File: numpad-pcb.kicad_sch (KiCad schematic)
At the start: 20 parts, among them J1 AVR-ISP-6, SW1 SW_Push, U1 ATmega32U4-A, Y1 Crystal_GND24_Small

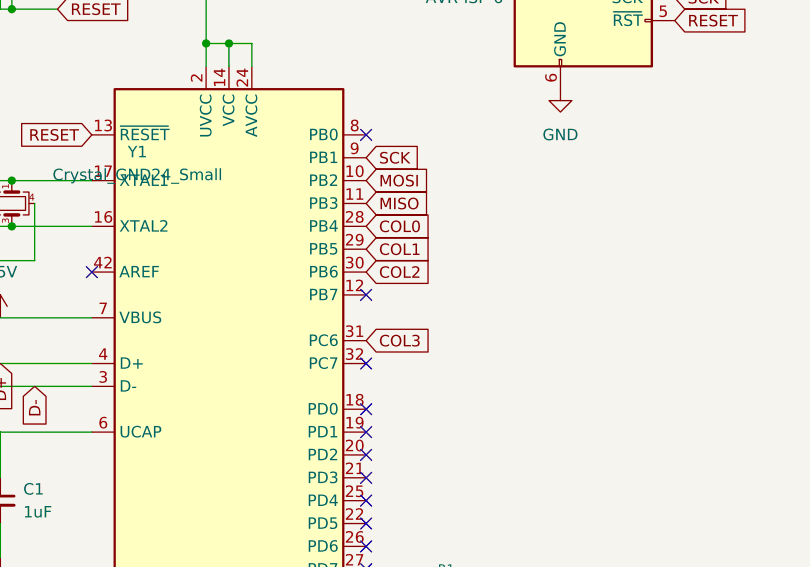
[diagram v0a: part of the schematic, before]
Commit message: Finish traces and start silkscreen
Still need to modify traces to be more optimal and increase readibility.
Also updated silkscreen preferences locally to have the label of each
switch on both the front and back of the PCB. Need to make a note that
this change is local because of the submodule imported from the start.
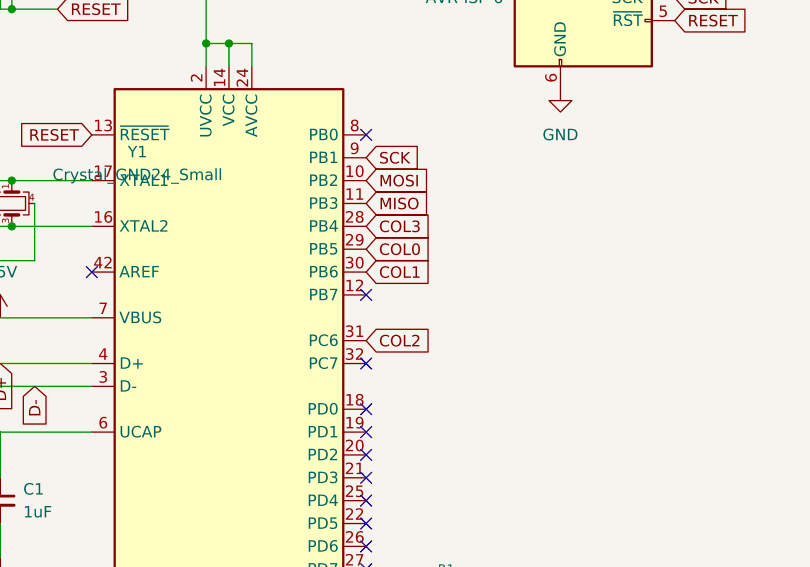
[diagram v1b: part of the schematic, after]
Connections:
- net COL0: now also U1.29 (PB5); no longer U1.28 (PB4)
- net COL1: now also U1.30 (PB6); no longer U1.29 (PB5)
- net COL2: now also U1.31 (PC6); no longer U1.30 (PB6)
- net COL3: now also U1.28 (PB4); no longer U1.31 (PC6)

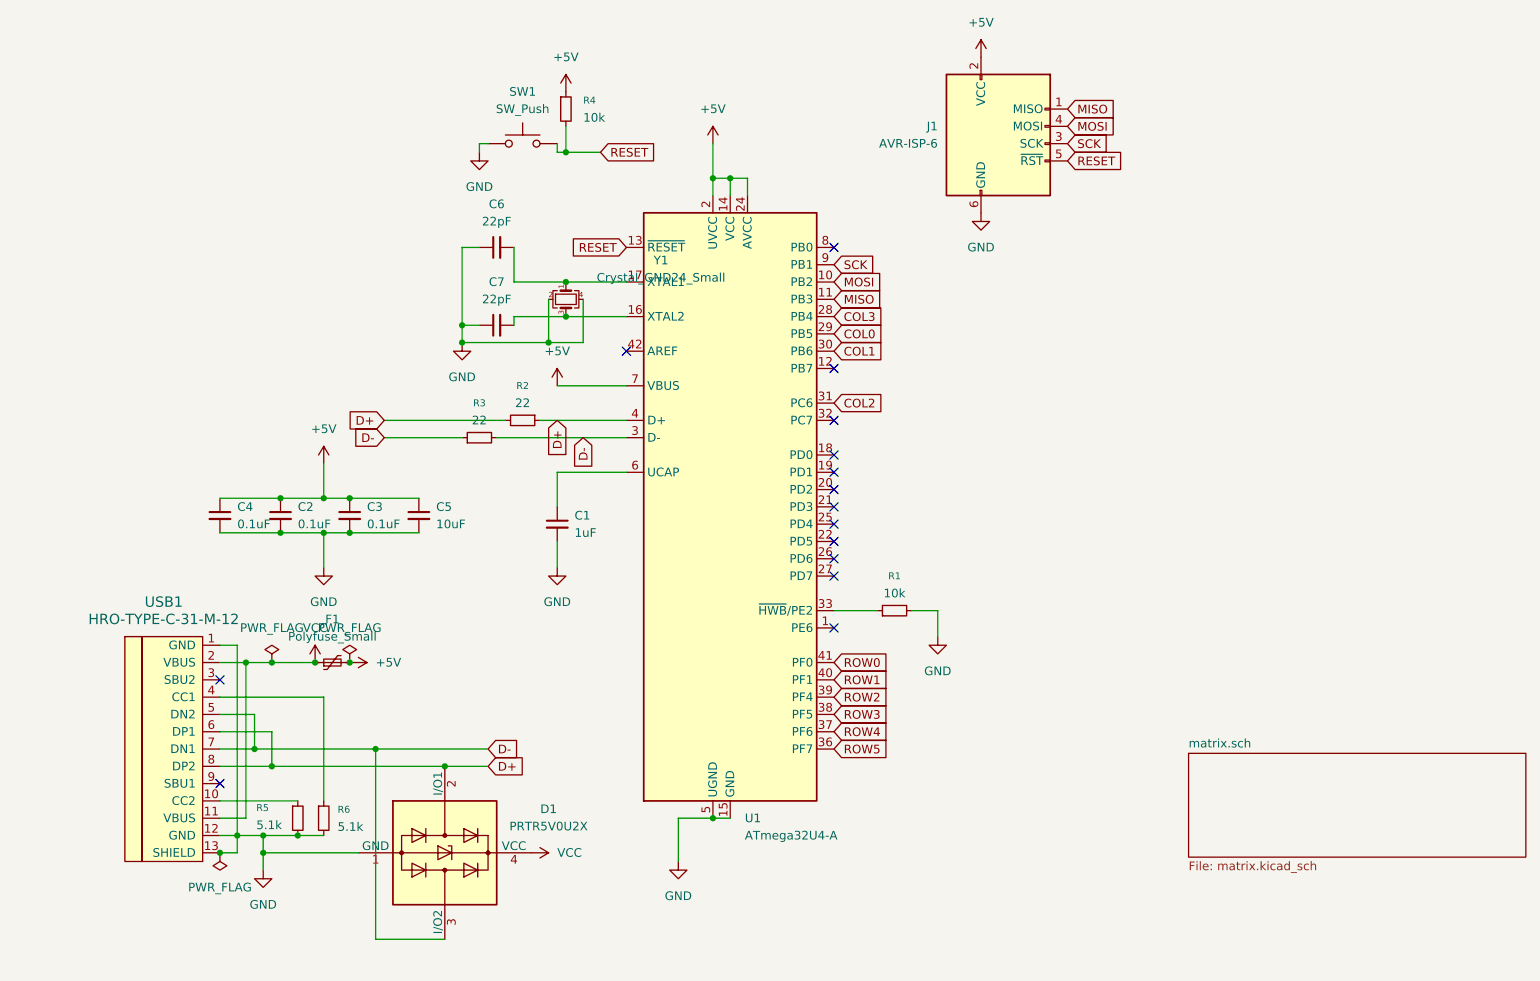
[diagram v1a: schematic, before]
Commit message: Add USB-C shield protection
Changed the USB-C shield from being connected to ground to being
connected to a ferrite bead low pass filter to manage ESD. Also adjusted
ground around USB to prevent ESD from damaging nearby components.
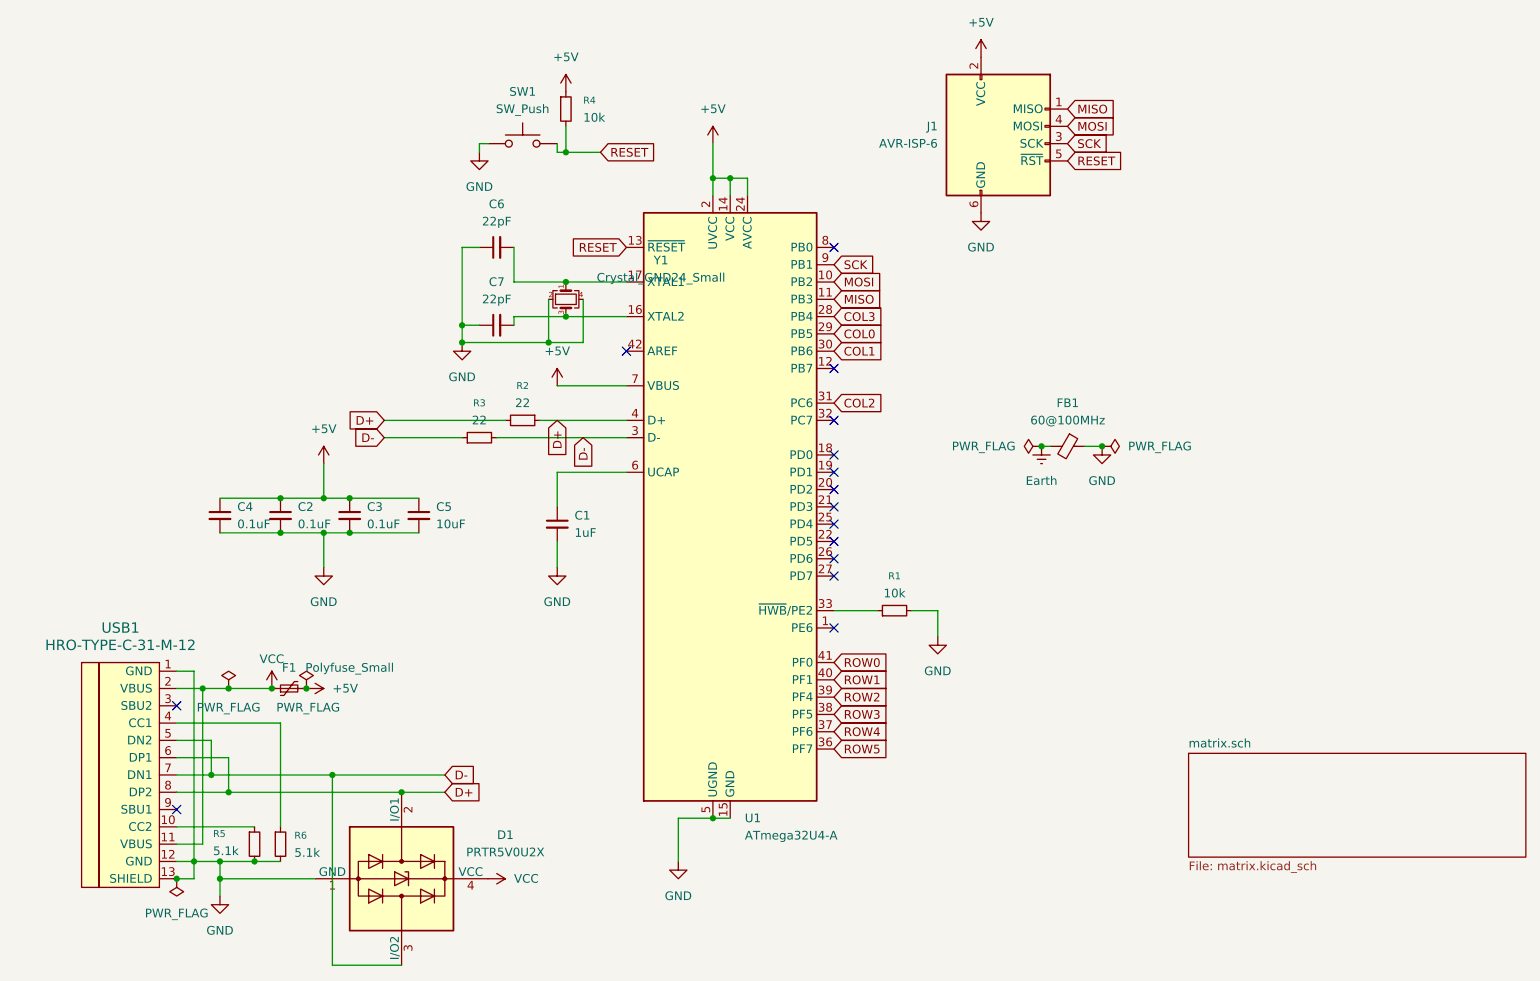
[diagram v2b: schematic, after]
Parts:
- added FB1: 60@100MHz, Inductor_SMD:L_0805_2012Metric_Pad1.15x1.40mm_HandSolder, symbol Device:FerriteBead_Small
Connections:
- net GND: now also FB1.1
- new net Earth: FB1.2
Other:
- moved on the sheet: D1, F1, R5, R6, USB1
